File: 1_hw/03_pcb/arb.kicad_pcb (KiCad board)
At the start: 4 copper layers, 100 x 100 mm, 269 parts, among them J1 TYPE-C-31-M-12, J2 SMA, J3 SMA, J4 BNC, J5 PH-00244, SW1 TS-1187A-B-A-B, SW2 SS-12D02-VG4, SW3 SS-12D02-VG4, U1 TLV70333DBV, U10 LMK1C1103PWR, U11 STM32F446ZETx, U12 ICE40UP5K-SG48ITR, U13 93LC56BT-I_OT, U14 FT2232HL, U15 W25Q128JVSIQ, U16 W25Q128JVSIQ, U17 AD9850, U18 AD9744, U19 LM6171, U2 TLV76133DCY, U20 LM6171, U21 TMUX6104, U22 TPL0401B-10, U23 THS3491, U24 ADG1219BRJZ, U25 LM6171, U26 TMUX6104, U3 TLV70333DBV, U4 LM3880MF-1AA, U5 TLV70312DBV, U6 TLV70325DBV, U7 TPS65131RGE, U8 TPD2E001DRL, U9 ADG1219BRJZ, X1 ASE-10.000MHz, X2 ASE-100.000MHz, Y1 32.768k, Y2 12 MHz

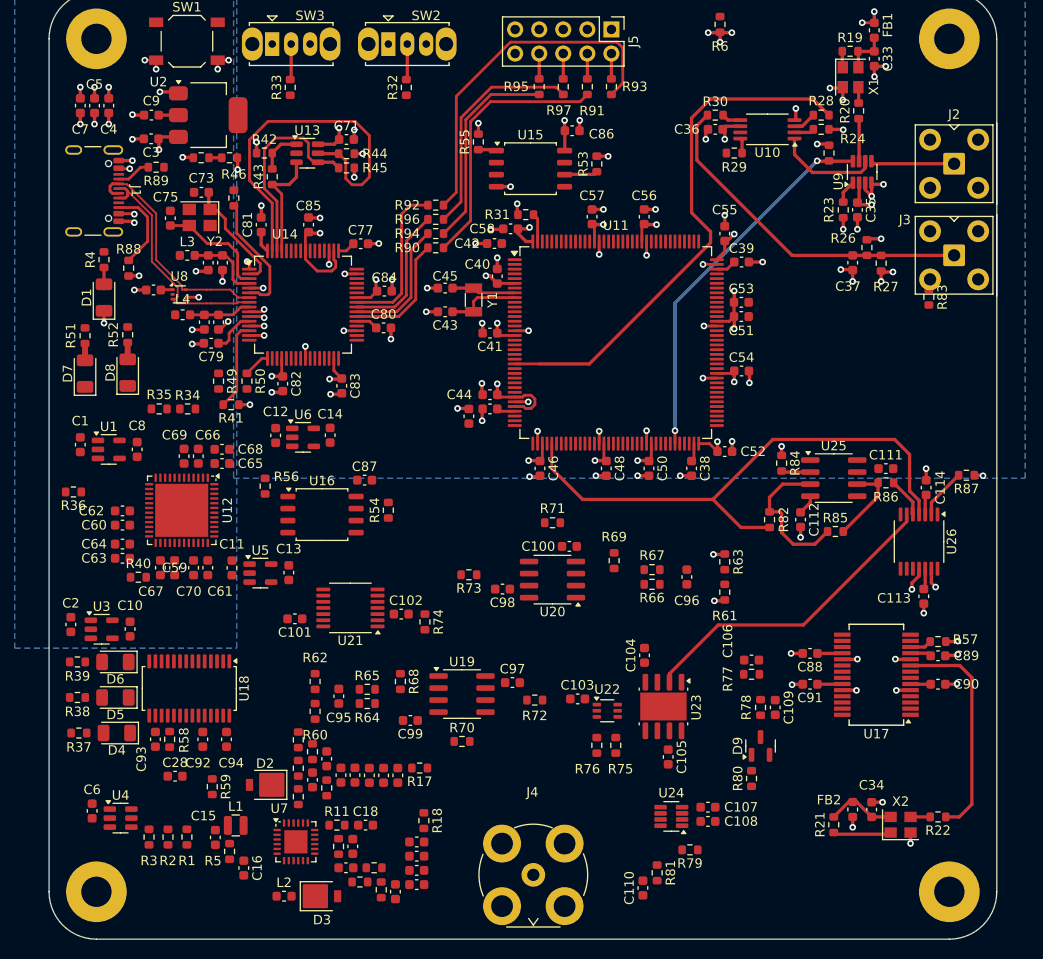
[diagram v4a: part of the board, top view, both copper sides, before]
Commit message: FEAT: Laid out some more analog. Laid out FPGA and DDC ICs.
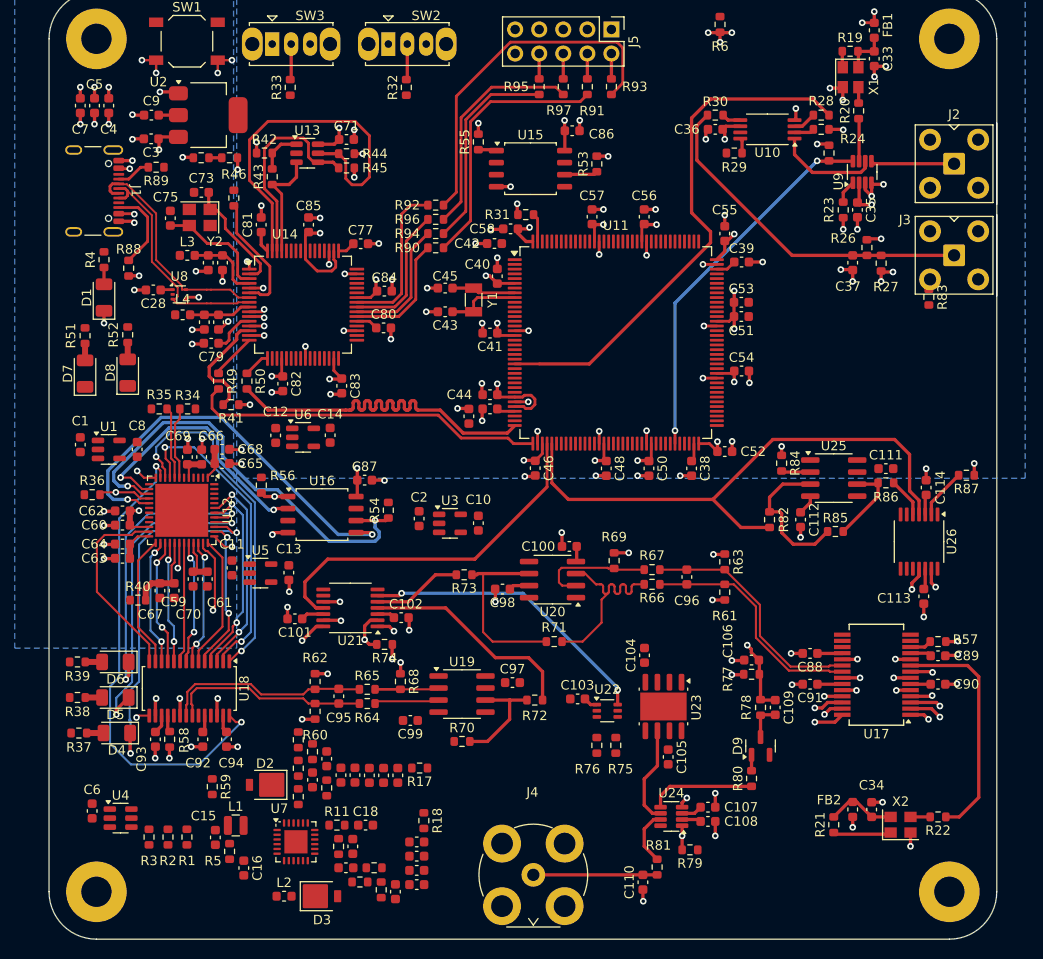
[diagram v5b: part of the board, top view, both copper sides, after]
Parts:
- removed the C28 at (114.0, 125.8)
- removed the C28 at (111.7, 74.5)
- added C28: 100n, Capacitor_SMD:C_0603_1608Metric, F.Cu at (111.7, 74.5)
- moved C10 38.4 mm to (146.0, 99.0)
- moved C2 38.4 mm to (139.8, 98.6)
- moved U3 38.4 mm to (143.0, 99.1)
- moved R71 12.5 mm to (154.0, 111.5)
- moved R74 4.88 mm to (136.1, 111.8), turned to 180 degrees
- moved C67 2.41 mm to (112.4, 106.2)
- moved C70 2.41 mm to (113.9, 106.2)
- moved R40 2.41 mm to (110.1, 107.2)
- moved R36 2.00 mm to (105.2, 96.0)
- moved C59 1.19 mm to (115.9, 105.0)
- moved C61 1.19 mm to (117.4, 105.0)
- moved C110 0.61 mm to (163.4, 136.9)
- moved R81 0.61 mm to (164.9, 135.3), turned to 90 degrees
- moved C46 0.50 mm to (152.0, 93.2)
- moved R73 0.50 mm to (144.5, 104.5)
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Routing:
- net GND: track 141.3 -> 192.4 mm, vias 108 -> 143
- net GPIO_DACCLK_FPGA_DAC_3P3: track 0.00 -> 50.9 mm, vias 0 -> 2
- net SPI_SCLK_MCU_FPGA_3P3: track 0.00 -> 47.5 mm, vias 0 -> 2
- net SPI_MOSI_MCU_FPGA_3P3: track 0.00 -> 44.3 mm, vias 0 -> 2
- net UART_MCUTX_FTDIRX_3P3: track 0.00 -> 39.8 mm
- net GPIO_LED0_FPGA_LED_OD: track 0.00 -> 38.5 mm, vias 0 -> 2
- net ANALOG_DAC1_MCU_AMUX1: track 0.00 -> 38.3 mm
- net UART_FTDITX_MCURX_3P3: track 0.00 -> 37.7 mm
- net GPIO_DACB13_FPGA_DAC_3P3: track 0.00 -> 37.0 mm, vias 0 -> 2
- net GPIO_LED1_FPGA_LED_OD: track 0.00 -> 34.4 mm, vias 0 -> 2
- net GPIO_DACB12_FPGA_DAC_3P3: track 0.00 -> 33.1 mm, vias 0 -> 2
- net GPIO_LED2_FPGA_LED_OD: track 0.00 -> 31.3 mm, vias 0 -> 2
- net SPI_MISO_FPGA_MCU_3P3: track 0.00 -> 28.3 mm, vias 0 -> 2
- net ANALOG_DDS_OUT_N: track 0.00 -> 25.5 mm
- net ANALOG_DDS_OUT_P: track 0.00 -> 25.0 mm
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
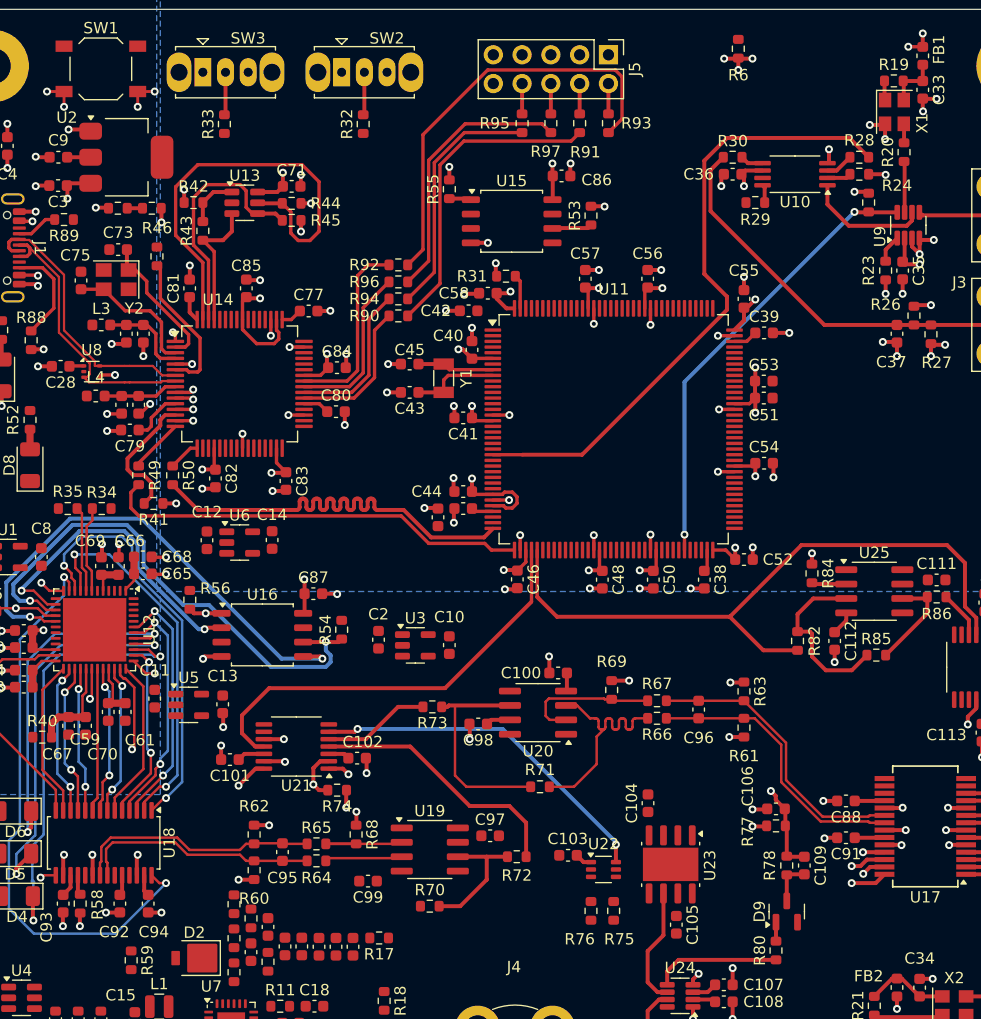
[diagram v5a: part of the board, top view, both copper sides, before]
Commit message: FEAT: Laid out JTAG, Processor QSPI. Length Matched JTAG.
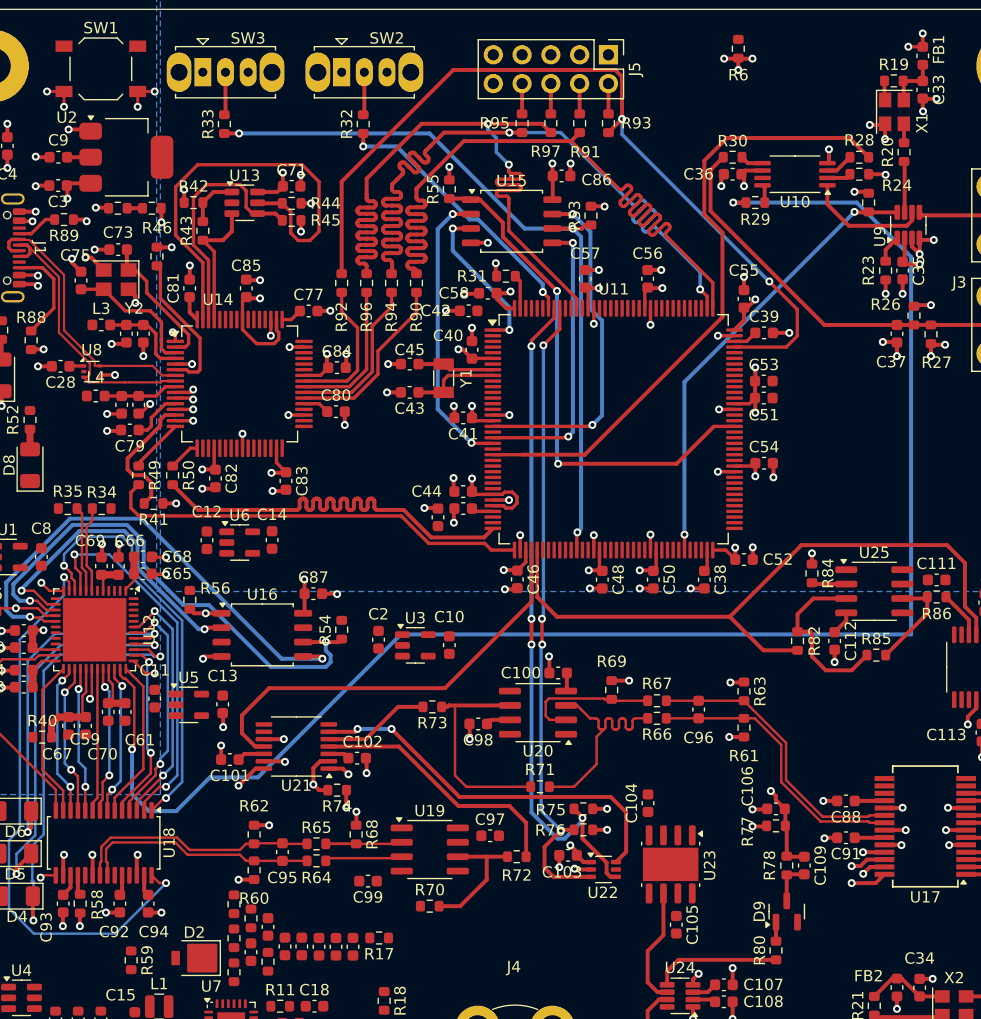
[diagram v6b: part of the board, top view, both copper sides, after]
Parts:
- moved R75 9.39 mm to (157.8, 113.5), turned to 0 degrees
- moved R76 7.18 mm to (157.8, 115.3), turned to 0 degrees
- moved R92 5.25 mm to (136.5, 67.1), turned to -90 degrees
- moved R90 3.31 mm to (143.1, 67.1), turned to -90 degrees
- moved R96 2.80 mm to (138.7, 67.1), turned to -90 degrees
- moved R94 1.52 mm to (140.9, 67.1), turned to -90 degrees
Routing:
- net CLK_10MHZ_DIST_FPGA_3P3: track 7.81 -> 139.7 mm, vias 1 -> 2
- net GPIO_BOOT1_SW_MCU_3P3_L: track 3.53 -> 66.6 mm, vias 0 -> 3
- net I2C_SDA_MCU_POT_3P3: track 0.00 -> 59.6 mm, vias 0 -> 4
- net I2C_SCL_MCU_POT_3P3: track 0.00 -> 57.0 mm, vias 0 -> 4
- net JTAG_MCU_TDI_3P3: track 21.8 -> 71.6 mm, vias 0 -> 2
- net JTAG_MCU_TDO_3P3: track 23.9 -> 68.1 mm, vias 0 -> 2
- net QSPI_NCS_MCU_FLASH_3P3: track 1.94 -> 45.8 mm, vias 0 -> 2
- net JTAG_MCU_TCK_3P3: track 28.0 -> 71.0 mm
- net JTAG_MCU_TMS_3P3: track 37.7 -> 74.1 mm, vias 0 -> 2
- net QSPI_IO3_MCU_FLASH_3P3: track 0.00 -> 30.7 mm, vias 0 -> 2
- net QSPI_IO0_MCU_FLASH_3P3: track 0.00 -> 25.8 mm, vias 0 -> 2
- net QSPI_IO1_MCU_FLASH_3P3: track 0.00 -> 25.6 mm, vias 0 -> 2
- net GPIO_BOOT0_SW_MCU_3P3_L: track 0.00 -> 24.4 mm, vias 0 -> 2
- net QSPI_IO2_MCU_FLASH_3P3: track 0.00 -> 14.1 mm, vias 0 -> 2
- net GND: track 192.4 -> 203.8 mm, vias 143 -> 151
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
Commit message: FEAT: Laid out MCU DDS. Changed some MCU Pins for better routability.
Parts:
- moved R83 25.5 mm to (175.8, 93.5), turned to 0 degrees
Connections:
- U11 pad 13: GPIO_EN_MCU_AMUX3_3P3 -> unconnected-(U11-PF3-Pad13)
- U11 pad 14: GPIO_SEL1_MCU_AMUX3_3P3 -> unconnected-(U11-PF4-Pad14)
- U11 pad 15: GPIO_SEL0_MCU_AMUX3_3P3 -> unconnected-(U11-PF5-Pad15)
- U11 pad 56: unconnected-(U11-PG0-Pad56) -> GPIO_AMP-PD_MCU_AMP2_3P3
- U11 pad 63: GPIO_AMP-PD_MCU_AMP2_3P3 -> unconnected-(U11-PE10-Pad63)
- U11 pad 88: unconnected-(U11-PG3-Pad88) -> GPIO_EN_MCU_AMUX3_3P3
- U11 pad 89: unconnected-(U11-PG4-Pad89) -> GPIO_SEL1_MCU_AMUX3_3P3
- U11 pad 90: unconnected-(U11-PG5-Pad90) -> GPIO_SEL0_MCU_AMUX3_3P3
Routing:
- net GPIO_W-CLK_MCU_DDS_3P3: track 1.78 -> 72.6 mm, vias 1 -> 2
- net GPIO_D0_MCU_DDS_3P3: track 2.32 -> 71.7 mm, vias 1 -> 2
- net GPIO_D2_MCU_DDS_3P3: track 3.47 -> 72.7 mm, vias 1 -> 2
- net GPIO_D3_MCU_DDS_3P3: track 2.10 -> 70.4 mm, vias 1 -> 2
- net GPIO_D1_MCU_DDS_3P3: track 3.26 -> 70.2 mm, vias 1 -> 2
- net GPIO_RST_MCU_DDS_3P3: track 1.88 -> 68.3 mm, vias 1 -> 2
- net GPIO_D4_MCU_DDS_3P3: track 3.22 -> 63.2 mm, vias 1 -> 2
- net GPIO_D5_MCU_DDS_3P3: track 2.13 -> 60.1 mm, vias 1 -> 2
- net GPIO_D7_MCU_DDS_3P3: track 1.90 -> 59.1 mm, vias 1 -> 2
- net GPIO_SEL_MCU_AMUX2_3P3: track 0.00 -> 57.2 mm, vias 0 -> 2
- net GPIO_D6_MCU_DDS_3P3: track 3.14 -> 59.3 mm, vias 1 -> 2
- net GPIO_FQ-UD_MCU_DDS_3P3: track 2.36 -> 53.5 mm, vias 1 -> 2
- net GPIO_100M-EN_MCU_100M-OSC_3P3: track 6.14 -> 55.2 mm, vias 0 -> 2
- net GPIO_SEL1_MCU_AMUX3_3P3: track 0.00 -> 43.3 mm
- net ANALOG_DC-OFFSET_AMUX3_AMP3: track 34.2 -> 76.8 mm
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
